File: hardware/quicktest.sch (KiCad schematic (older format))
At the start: 47 parts

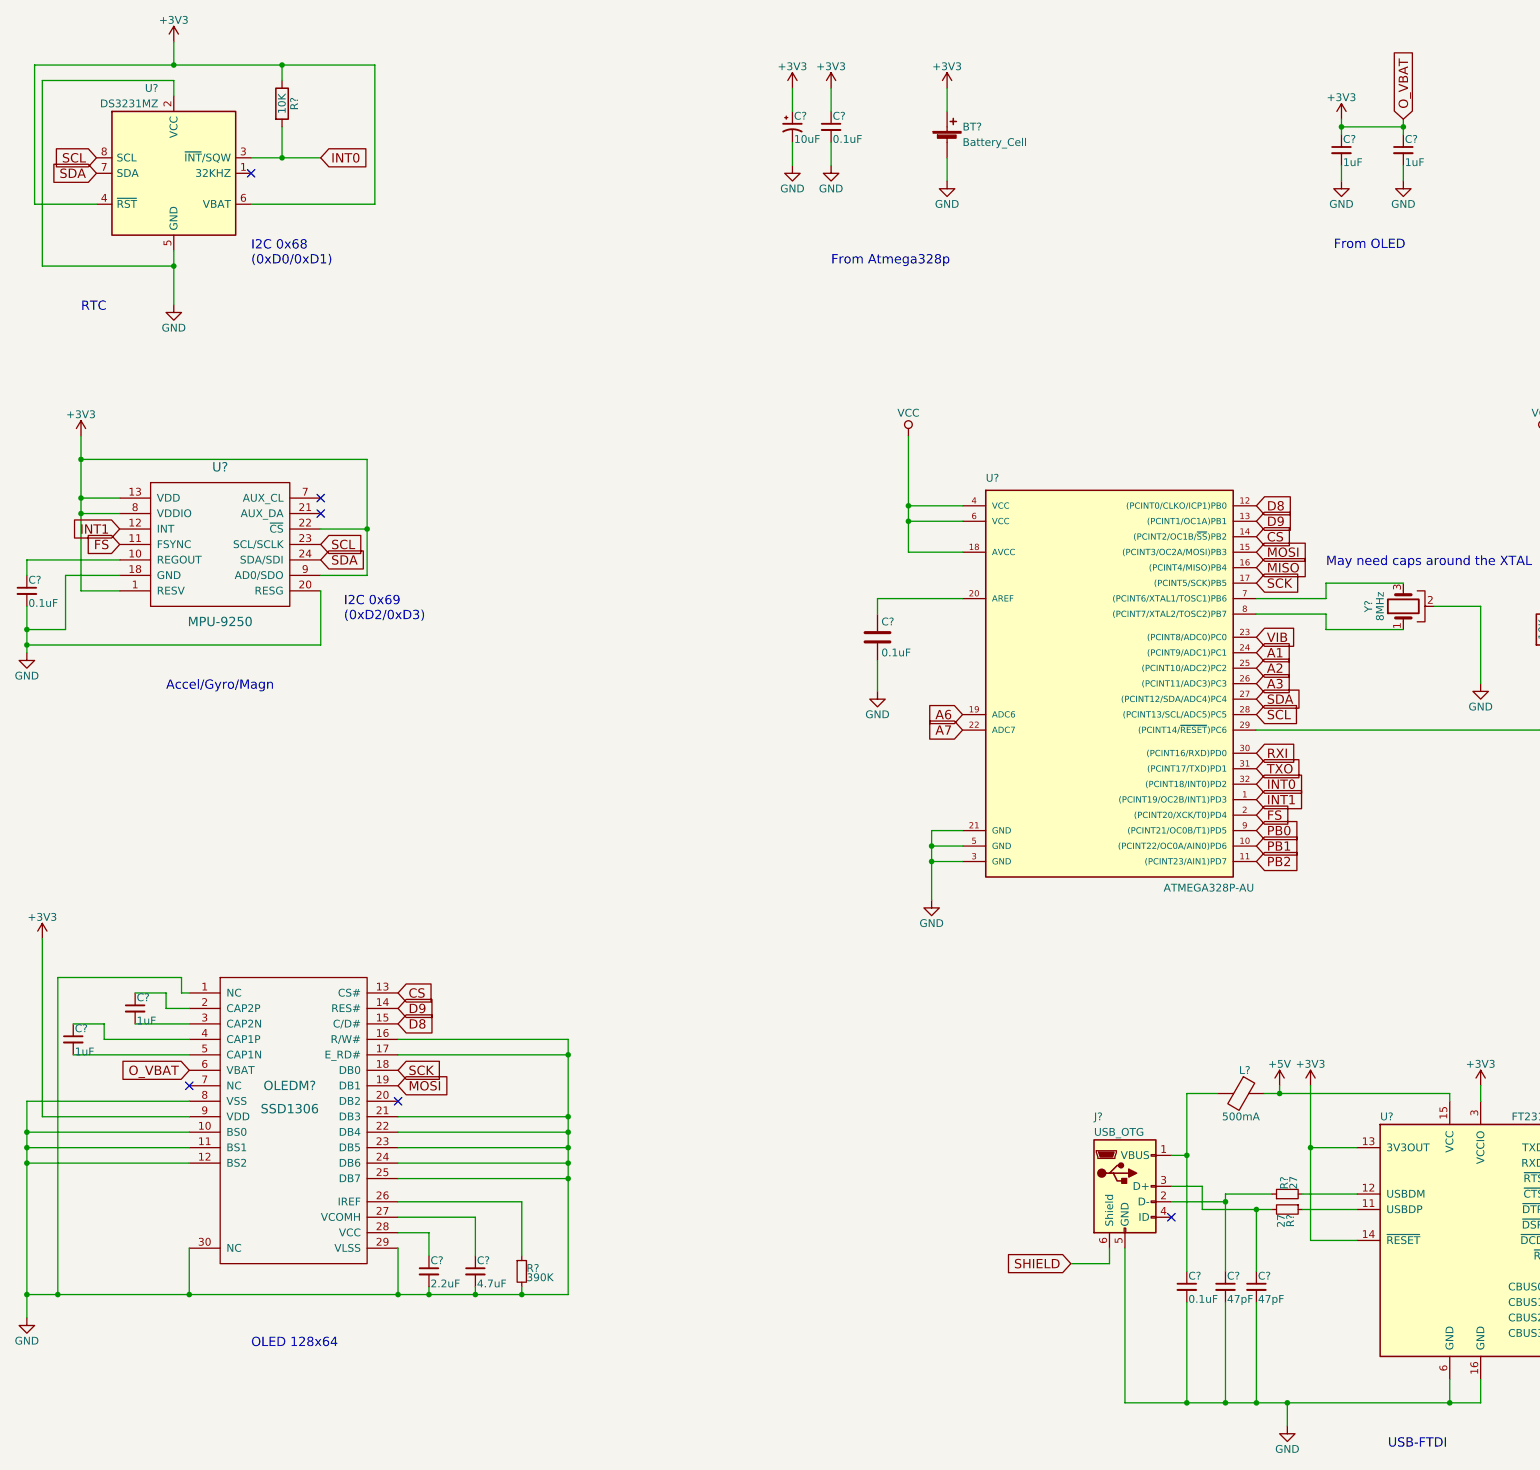
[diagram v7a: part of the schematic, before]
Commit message: figured out the power supply circuitry. adding in caps close to the power supply to each IC
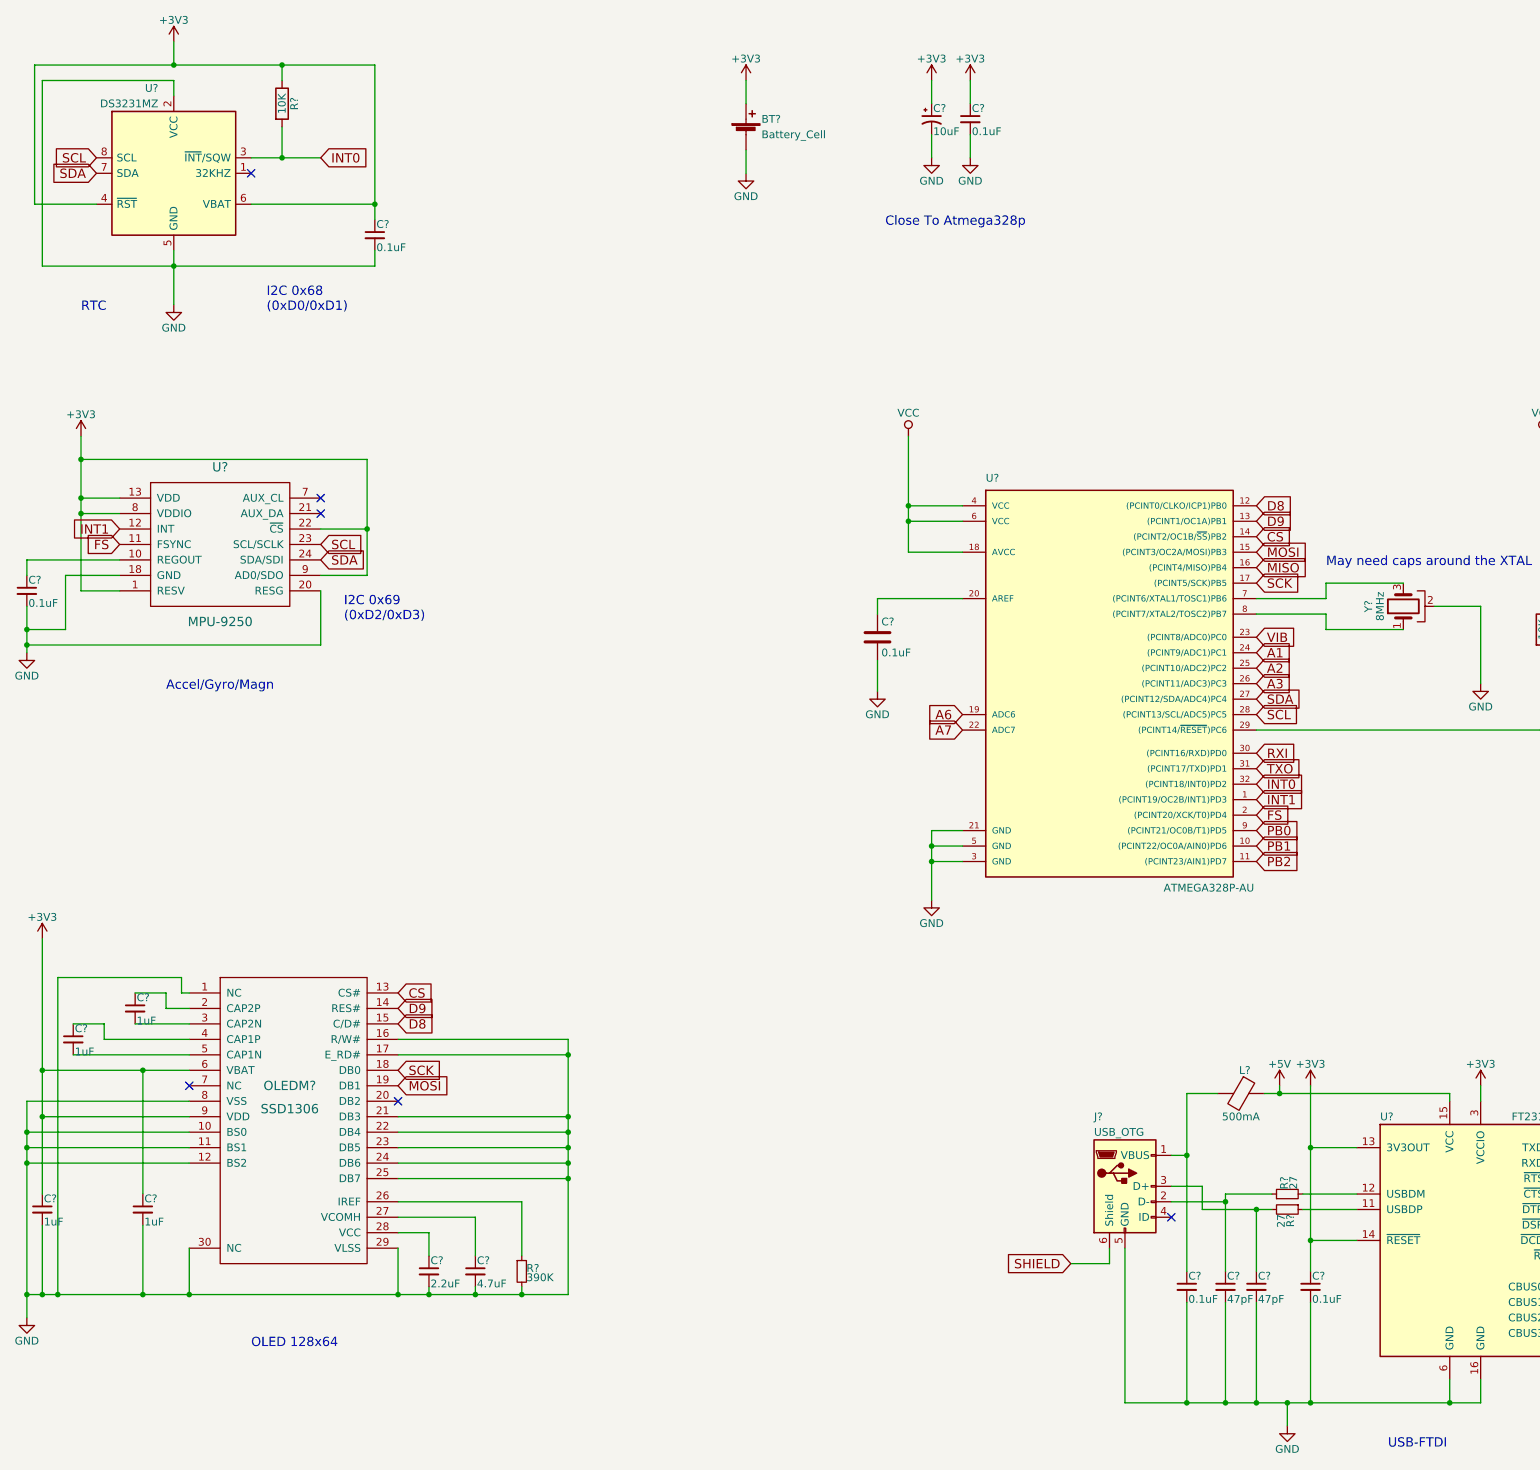
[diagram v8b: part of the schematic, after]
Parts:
- removed C? (x2): 1uF, symbol C_Small
- added C? (x2): 1uF, symbol C_Small
- added C? (x2): 0.1uF, symbol C_Small
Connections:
- net +3V3: now also C?.1, C?.1, C?.1, C?.1
- net GND: now also C?.2, C?.2, C?.2, C?.2
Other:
- note added: "Close To Atmega328p"
- note removed: "From Atmega328p"
- note removed: "From OLED"
- moved on the sheet: BT?, C?
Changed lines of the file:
@@
 L +3V3 #PWR?
 U 1 1 596E0DE2
-P 6000 1150
-F 0 "#PWR?" H 6000 1000 50  0001 C CNN
-F 1 "+3V3" H 6000 1290 50  0000 C CNN
-F 2 "" H 6000 1150 50  0001 C CNN
-F 3 "" H 6000 1150 50  0001 C CNN
-	1    6000 1150
+P 6900 1100
+F 0 "#PWR?" H 6900 950 50  0001 C CNN
+F 1 "+3V3" H 6900 1240 50  0000 C CNN
+F 2 "" H 6900 1100 50  0001 C CNN
+F 3 "" H 6900 1100 50  0001 C CNN
+	1    6900 1100
 	1    0    0    -1
 $EndComp
@@
 L C_Small C?
 U 1 1 596E0E19
-P 6000 1400
-F 0 "C?" H 6010 1470 50  0000 L CNN
-F 1 "0.1uF" H 6010 1320 50  0000 L CNN
-F 2 "" H 6000 1400 50  0001 C CNN
-F 3 "" H 6000 1400 50  0001 C CNN
-	1    6000 1400
+P 6900 1350
+F 0 "C?" H 6910 1420 50  0000 L CNN
+F 1 "0.1uF" H 6910 1270 50  0000 L CNN
+F 2 "" H 6900 1350 50  0001 C CNN
+F 3 "" H 6900 1350 50  0001 C CNN
+	1    6900 1350
 	1    0    0    -1
 $EndComp
@@
 L CP1_Small C?
 U 1 1 596E0E9E
-P 5750 1400
-F 0 "C?" H 5760 1470 50  0000 L CNN
-F 1 "10uF" H 5760 1320 50  0000 L CNN
-F 2 "" H 5750 1400 50  0001 C CNN
-F 3 "" H 5750 1400 50  0001 C CNN
-	1    5750 1400
+P 6650 1350
+F 0 "C?" H 6660 1420 50  0000 L CNN
+F 1 "10uF" H 6660 1270 50  0000 L CNN
+F 2 "" H 6650 1350 50  0001 C CNN
+F 3 "" H 6650 1350 50  0001 C CNN
+	1    6650 1350
 	1    0    0    -1
 $EndComp
@@
 L GND #PWR?
 U 1 1 596E0EF7
-P 5750 1650
-F 0 "#PWR?" H 5750 1400 50  0001 C CNN
-F 1 "GND" H 5750 1500 50  0000 C CNN
-F 2 "" H 5750 1650 50  0001 C CNN
-F 3 "" H 5750 1650 50  0001 C CNN
-	1    5750 1650
+P 6650 1600
+F 0 "#PWR?" H 6650 1350 50  0001 C CNN
+F 1 "GND" H 6650 1450 50  0000 C CNN
+F 2 "" H 6650 1600 50  0001 C CNN
+F 3 "" H 6650 1600 50  0001 C CNN
+	1    6650 1600
 	1    0    0    -1
 $EndComp
@@
 L GND #PWR?
 U 1 1 596E0F1D
-P 6000 1650
-F 0 "#PWR?" H 6000 1400 50  0001 C CNN
-F 1 "GND" H 6000 1500 50  0000 C CNN
-F 2 "" H 6000 1650 50  0001 C CNN
-F 3 "" H 6000 1650 50  0001 C CNN
-	1    6000 1650
+P 6900 1600
+F 0 "#PWR?" H 6900 1350 50  0001 C CNN
+F 1 "GND" H 6900 1450 50  0000 C CNN
+F 2 "" H 6900 1600 50  0001 C CNN
+F 3 "" H 6900 1600 50  0001 C CNN
+	1    6900 1600
 	1    0    0    -1
 $EndComp
@@
 L Battery_Cell BT?
 U 1 1 596E4236
-P 6750 1500
-F 0 "BT?" H 6850 1600 50  0000 L CNN
-F 1 "Battery_Cell" H 6850 1500 50  0000 L CNN
-F 2 "" V 6750 1560 50  0001 C CNN
-F 3 "" V 6750 1560 50  0001 C CNN
-	1    6750 1500
+P 5450 1450
+F 0 "BT?" H 5550 1550 50  0000 L CNN
+F 1 "Battery_Cell" H 5550 1450 50  0000 L CNN
+F 2 "" V 5450 1510 50  0001 C CNN
+F 3 "" V 5450 1510 50  0001 C CNN
+	1    5450 1450
 	1    0    0    -1
 $EndComp
@@
 L +3V3 #PWR?
 U 1 1 596E42B5
-P 6750 1150
-F 0 "#PWR?" H 6750 1000 50  0001 C CNN
-F 1 "+3V3" H 6750 1290 50  0000 C CNN
-F 2 "" H 6750 1150 50  0001 C CNN
-F 3 "" H 6750 1150 50  0001 C CNN
-	1    6750 1150
+P 5450 1100
+F 0 "#PWR?" H 5450 950 50  0001 C CNN
+F 1 "+3V3" H 5450 1240 50  0000 C CNN
+F 2 "" H 5450 1100 50  0001 C CNN
+F 3 "" H 5450 1100 50  0001 C CNN
+	1    5450 1100
 	1    0    0    -1
 $EndComp
@@
 L GND #PWR?
 U 1 1 596E42F6
-P 6750 1750
-F 0 "#PWR?" H 6750 1500 50  0001 C CNN
-F 1 "GND" H 6750 1600 50  0000 C CNN
-F 2 "" H 6750 1750 50  0001 C CNN
-F 3 "" H 6750 1750 50  0001 C CNN
-	1    6750 1750
+P 5450 1700
+F 0 "#PWR?" H 5450 1450 50  0001 C CNN
+F 1 "GND" H 5450 1550 50  0000 C CNN
+F 2 "" H 5450 1700 50  0001 C CNN
+F 3 "" H 5450 1700 50  0001 C CNN
+	1    5450 1700
 	1    0    0    -1
 $EndComp
@@
 $EndComp
 NoConn ~ 2250 1700
-Text Notes 2250 2300 0    60   ~ 0
+Text Notes 2350 2600 0    60   ~ 0
 I2C 0x68\n(0xD0/0xD1)
 $Comp
@@
 	10600 4800 10600 5300
 Wire Wire Line
-	5750 1650 5750 1500
-Wire Wire Line
-	6000 1650 6000 1500
-Wire Wire Line
-	6750 1750 6750 1600
-Wire Wire Line
-	6750 1300 6750 1150
+	6650 1600 6650 1450
+Wire Wire Line
+	6900 1600 6900 1450
+Wire Wire Line
+	5450 1700 5450 1550
+Wire Wire Line
+	5450 1250 5450 1100
 Wire Wire Line
 	14200 5950 14200 6350
@@
 	2250 1900 3050 1900
 Wire Wire Line
-	3050 1900 3050 1000
+	3050 1000 3050 2000
 Connection ~ 2450 1000
 Wire Wire Line
@@
 	900  1100 900  2300
 Wire Wire Line
-	900  2300 1750 2300
+	900  2300 3050 2300
 Connection ~ 1750 2300
 Wire Wire Line
@@
 	1850 7800 900  7800
 Wire Wire Line
-	900  7800 900  6650
+	900  6650 900  8300
 Wire Wire Line
 	1850 7900 800  7900
@@
 Wire Wire Line
 	1300 7200 1100 7200
-$Comp
-L +3V3 #PWR?
-U 1 1 59743AA2
-P 9300 1350
-F 0 "#PWR?" H 9300 1200 50  0001 C CNN
-F 1 "+3V3" H 9300 1490 50  0000 C CNN
-F 2 "" H 9300 1350 50  0001 C CNN
-F 3 "" H 9300 1350 50  0001 C CNN
-	1    9300 1350
-	1    0    0    -1
-$EndComp
-$Comp
-L C_Small C?
-U 1 1 59743AF0
-P 9300 1550
-F 0 "C?" H 9310 1620 50  0000 L CNN
-F 1 "1uF" H 9310 1470 50  0000 L CNN
-F 2 "" H 9300 1550 50  0001 C CNN
-F 3 "" H 9300 1550 50  0001 C CNN
-	1    9300 1550
-	1    0    0    -1
-$EndComp
-$Comp
-L GND #PWR?
-U 1 1 59743B4D
-P 9300 1750
-F 0 "#PWR?" H 9300 1500 50  0001 C CNN
-F 1 "GND" H 9300 1600 50  0000 C CNN
-F 2 "" H 9300 1750 50  0001 C CNN
-F 3 "" H 9300 1750 50  0001 C CNN
-	1    9300 1750
-	1    0    0    -1
-$EndComp
-Wire Wire Line
-	9300 1350 9300 1450
-Wire Wire Line
-	9300 1650 9300 1750
 Wire Wire Line
 	3200 8650 3200 8950
@@
 	3400 8950 3400 8900
 Connection ~ 3200 8950
-Text GLabel 1850 7500 0    60   Input ~ 0
-O_VBAT
-Text GLabel 9700 1350 1    60   Input ~ 0
-O_VBAT
-$Comp
-L C_Small C?
-U 1 1 597443AD
-P 9700 1550
-F 0 "C?" H 9710 1620 50  0000 L CNN
-F 1 "1uF" H 9710 1470 50  0000 L CNN
-F 2 "" H 9700 1550 50  0001 C CNN
-F 3 "" H 9700 1550 50  0001 C CNN
-	1    9700 1550
-	1    0    0    -1
-$EndComp
-$Comp
-L GND #PWR?
-U 1 1 5974448A
-P 9700 1750
-F 0 "#PWR?" H 9700 1500 50  0001 C CNN
-F 1 "GND" H 9700 1600 50  0000 C CNN
-F 2 "" H 9700 1750 50  0001 C CNN
-F 3 "" H 9700 1750 50  0001 C CNN
-	1    9700 1750
-	1    0    0    -1
-$EndComp
-Wire Wire Line
-	9700 1750 9700 1650
-Wire Wire Line
-	9700 1450 9700 1350
-Wire Wire Line
-	9700 1400 9300 1400
-Connection ~ 9300 1400
-Connection ~ 9700 1400
 $Comp
 L C_Small C?
@@
 	1    0    0    -1
 $EndComp
-Text Notes 6000 2300 0    60   ~ 0
-From Atmega328p
-Text Notes 9250 2200 0    60   ~ 0
-From OLED
+Text Notes 6350 2050 0    60   ~ 0
+Close To Atmega328p
 $Comp
 L Ferrite_Bead L?
@@
 	9400 8000 9100 8000
 Wire Wire Line
-	9100 7600 9100 8600
+	9100 7600 9100 8800
 Wire Wire Line
 	9100 8600 9400 8600
@@
 L +3V3 #PWR?
 U 1 1 598457E5
-P 5750 1150
-F 0 "#PWR?" H 5750 1000 50  0001 C CNN
-F 1 "+3V3" H 5750 1290 50  0000 C CNN
-F 2 "" H 5750 1150 50  0001 C CNN
-F 3 "" H 5750 1150 50  0001 C CNN
-	1    5750 1150
-	1    0    0    -1
-$EndComp
-Wire Wire Line
-	5750 1150 5750 1300
-Wire Wire Line
-	6000 1150 6000 1300
+P 6650 1100
+F 0 "#PWR?" H 6650 950 50  0001 C CNN
+F 1 "+3V3" H 6650 1240 50  0000 C CNN
+F 2 "" H 6650 1100 50  0001 C CNN
+F 3 "" H 6650 1100 50  0001 C CNN
+	1    6650 1100
+	1    0    0    -1
+$EndComp
+Wire Wire Line
+	6650 1100 6650 1250
+Wire Wire Line
+	6900 1100 6900 1250
+$Comp
+L C_Small C?
+U 1 1 5982EA22
+P 900 8400
+F 0 "C?" H 910 8470 50  0000 L CNN
+F 1 "1uF" H 910 8320 50  0000 L CNN
+F 2 "" H 900 8400 50  0001 C CNN
+F 3 "" H 900 8400 50  0001 C CNN
+	1    900  8400
+	1    0    0    -1
+$EndComp
+Connection ~ 900  7800
+Wire Wire Line
+	900  8500 900  8950
+Connection ~ 900  8950
+$Comp
+L C_Small C?
+U 1 1 5983459C
+P 1550 8400
+F 0 "C?" H 1560 8470 50  0000 L CNN
+F 1 "1uF" H 1560 8320 50  0000 L CNN
+F 2 "" H 1550 8400 50  0001 C CNN
+F 3 "" H 1550 8400 50  0001 C CNN
+	1    1550 8400
+	1    0    0    -1
+$EndComp
+Wire Wire Line
+	1550 8300 1550 7500
+Wire Wire Line
+	900  7500 1850 7500
+Connection ~ 900  7500
+Connection ~ 1550 7500
+Wire Wire Line
+	1550 8500 1550 8950
+Connection ~ 1550 8950
+$Comp
+L C_Small C?
+U 1 1 598353E1
+P 3050 2100
+F 0 "C?" H 3060 2170 50  0000 L CNN
+F 1 "0.1uF" H 3060 2020 50  0000 L CNN
+F 2 "" H 3050 2100 50  0001 C CNN
+F 3 "" H 3050 2100 50  0001 C CNN
+	1    3050 2100
+	1    0    0    -1
+$EndComp
+Connection ~ 3050 1900
+Wire Wire Line
+	3050 2300 3050 2200
+$Comp
+L C_Small C?
+U 1 1 598361EF
+P 9100 8900
+F 0 "C?" H 9110 8970 50  0000 L CNN
+F 1 "0.1uF" H 9110 8820 50  0000 L CNN
+F 2 "" H 9100 8900 50  0001 C CNN
+F 3 "" H 9100 8900 50  0001 C CNN
+	1    9100 8900
+	1    0    0    -1
+$EndComp
+Connection ~ 9100 8600
+Wire Wire Line
+	9100 9000 9100 9650
+Connection ~ 9100 9650
 $EndSCHEMATC
